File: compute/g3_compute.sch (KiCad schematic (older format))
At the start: 37 parts, among them J1 CPPC_Conn, J101 CONSMA001-SMD-G, J102 Temp_Connector_1x4, J2 Power_Subsystem_Conn, J3 GPIO_Breakout_Conn, U101 PA1616D, U102 LoRa-E5

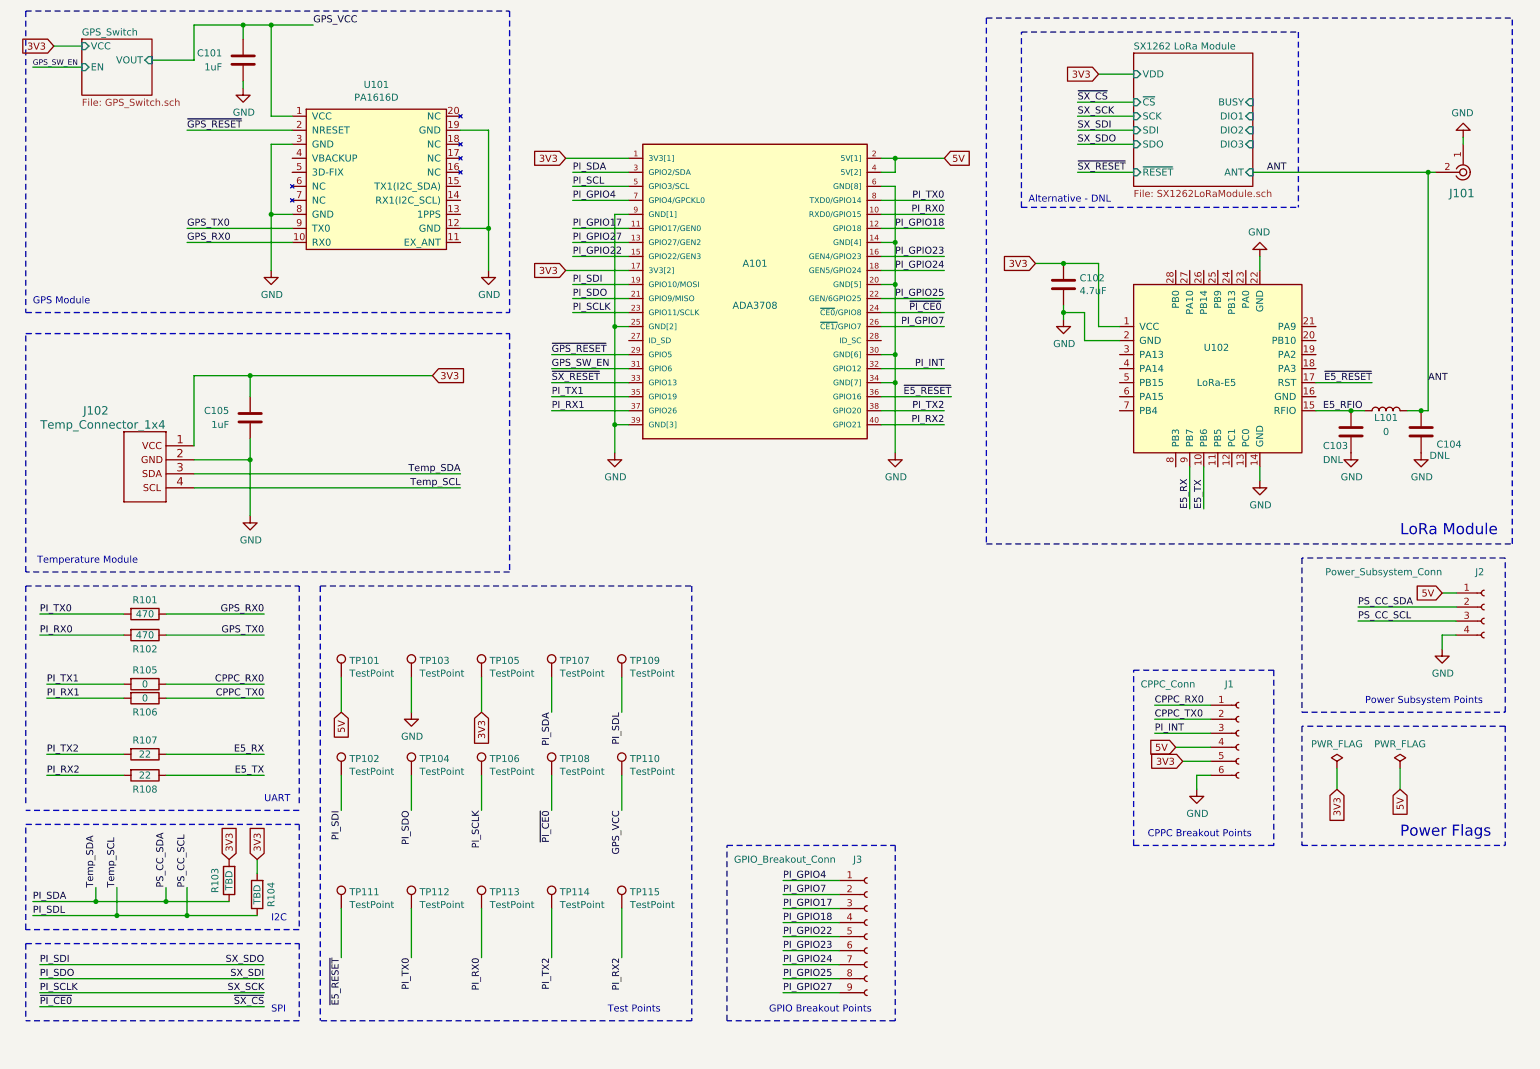
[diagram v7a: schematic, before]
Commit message: Updating Power subsystem BOM fields and board to board connector
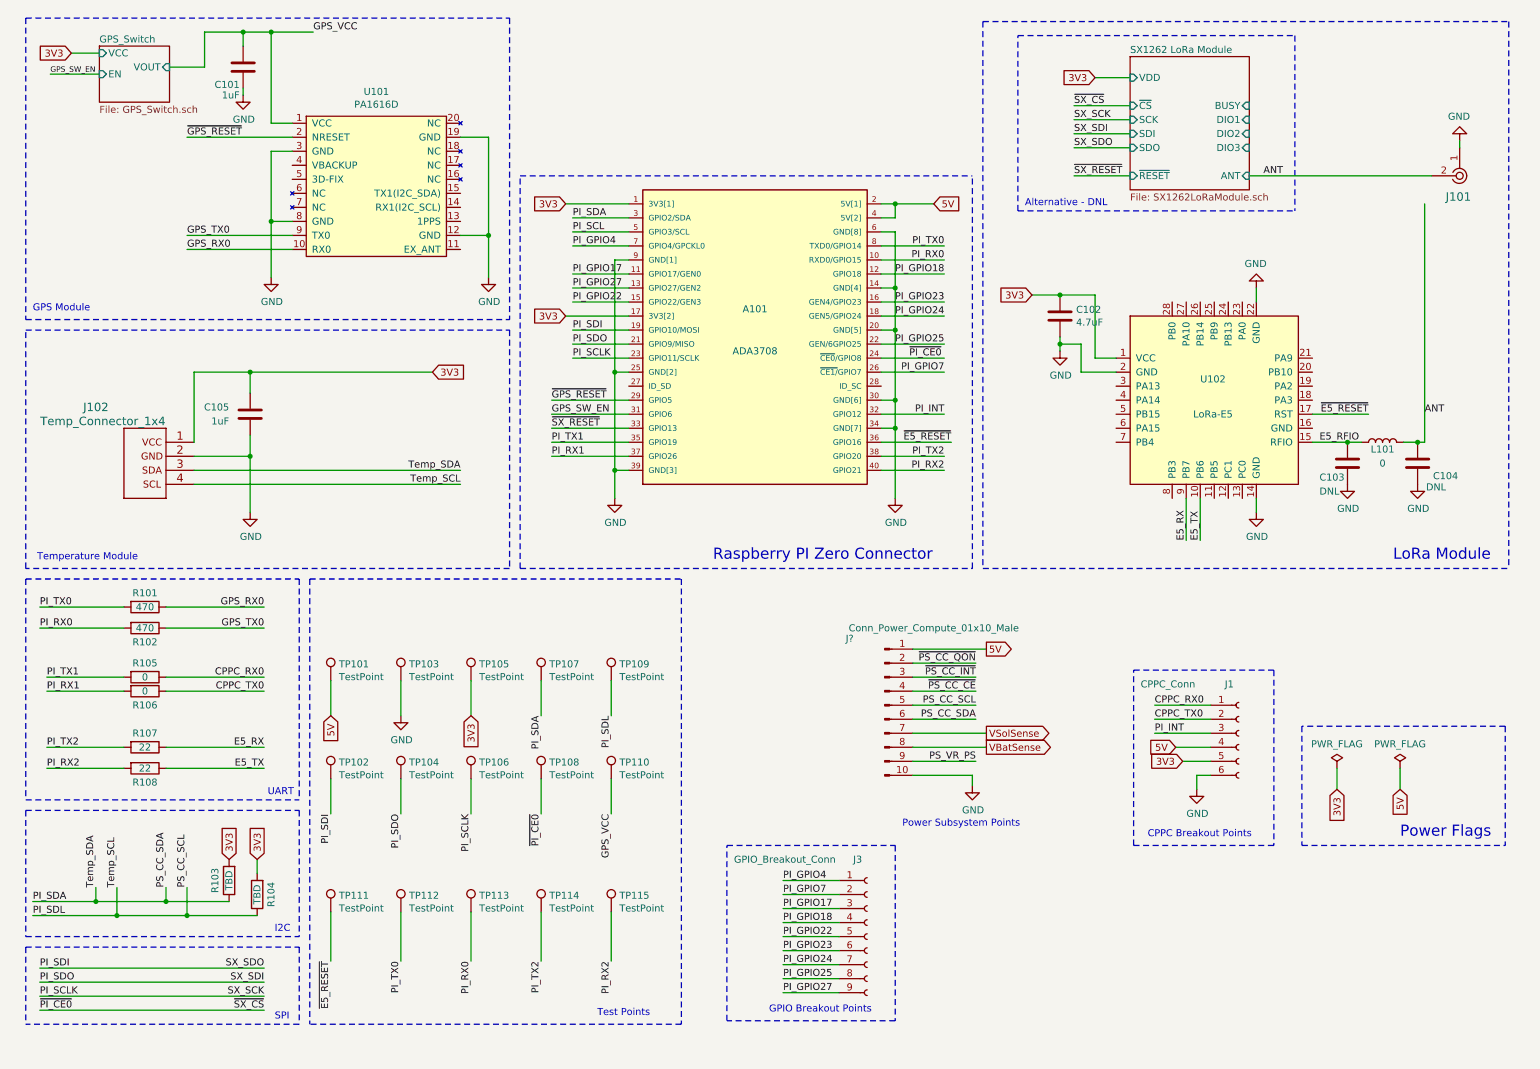
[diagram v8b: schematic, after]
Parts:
- removed J2: Power_Subsystem_Conn, Connector_Samtec_HLE_SMD:Samtec_HLE-102-02-xxx-DV_2x02_P2.54mm_Horizontal, symbol Connector:Conn_01x04_Female
- added J?: Conn_Power_Compute_01x10_Male, symbol Connector:Conn_01x10_Male
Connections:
- net 5V: now also J?.1 (Pin_1)
- net GND: now also J?.10 (Pin_10)
- net PI_SDA: now also J?.6 (Pin_6)
- net PI_SDL: now also J?.5 (Pin_5)
- new net PS_VR_PS: J?.9 (Pin_9)
- new net VBatSense: J?.8 (Pin_8)
- new net VSolSense: J?.7 (Pin_7)
- new net ~PS_CC_CE: J?.4 (Pin_4)
- new net ~PS_CC_INT: J?.3 (Pin_3)
- new net ~PS_CC_QON: J?.2 (Pin_2)
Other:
- note added: "Raspberry PI Zero Connector"
- moved on the sheet: A101, C101, C102, C103, C104, C105, J101, J102, L101, R101, R102, R105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
